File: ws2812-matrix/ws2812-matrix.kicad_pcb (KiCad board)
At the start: 2 copper layers, 80 x 80 mm, 268 parts, among them J1 Conn_01x03, J2 Conn_01x03

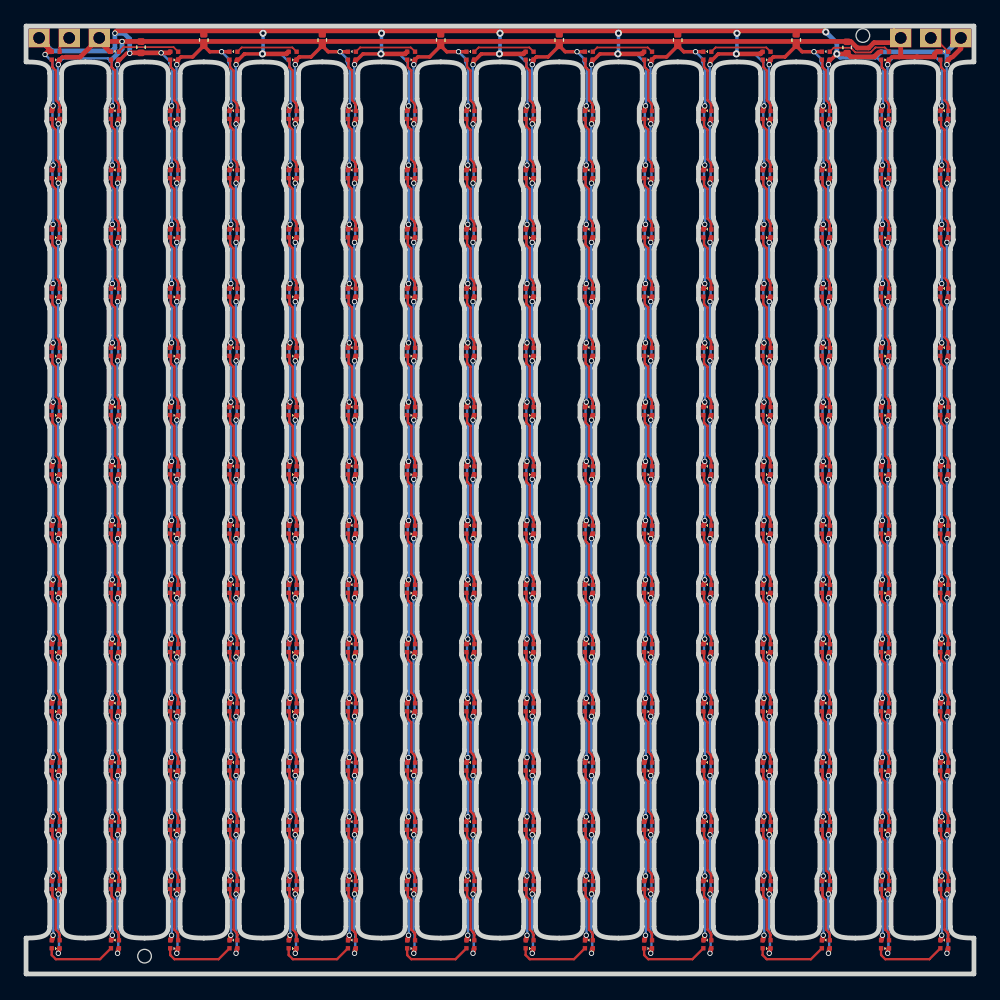
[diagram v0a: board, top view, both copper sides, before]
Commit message: ws2812-matrix: make connectors vertical, increase VCC/GND trace width
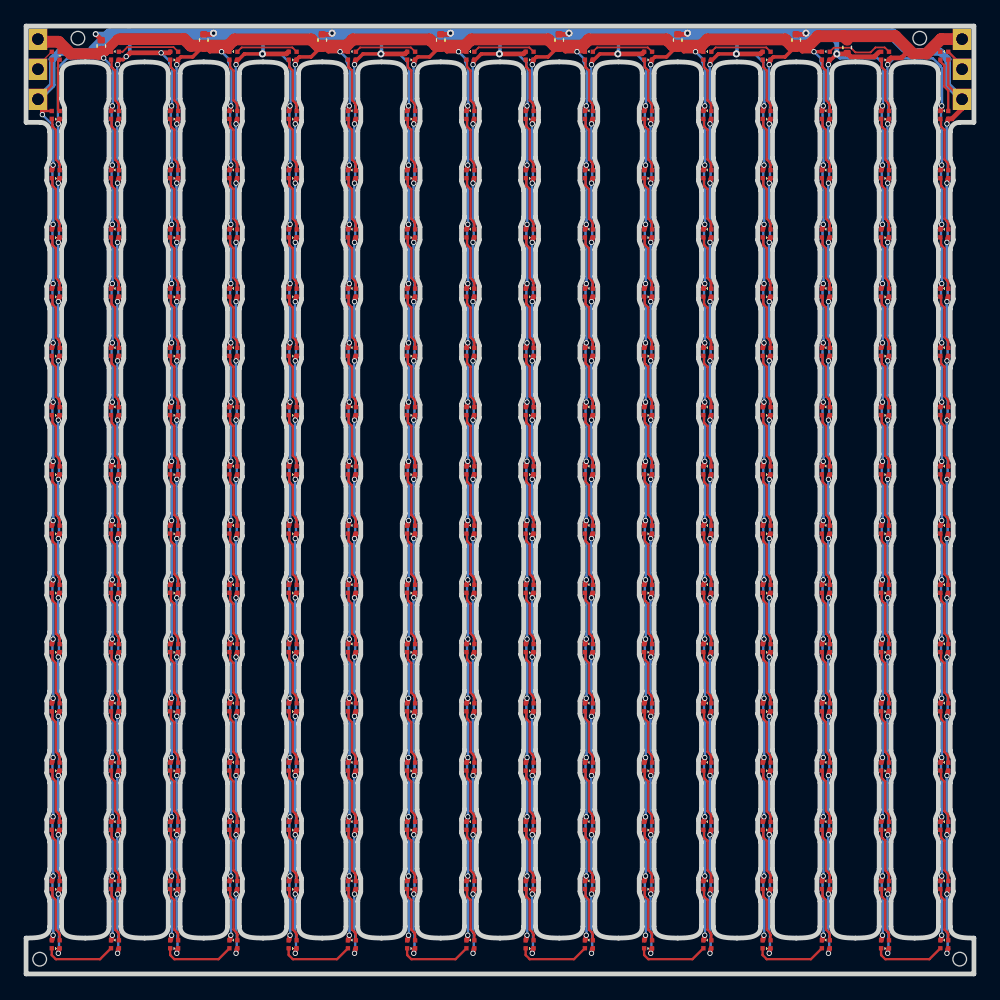
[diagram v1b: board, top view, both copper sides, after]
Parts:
- added REF**: ToolingHole_JLCPCB, Custom:ToolingHole_JLCPCB, F.Cu at (51.9, 48.5)
- added REF**: ToolingHole_JLCPCB, Custom:ToolingHole_JLCPCB, F.Cu at (126.3, 126.2)
- moved REF** 8.85 mm to (48.6, 126.3)
- moved J1 5.18 mm to (48.5, 53.7), turned to 90 degrees
- moved J2 5.18 mm to (126.5, 53.7), turned to 90 degrees
- moved REF** 4.81 mm to (122.9, 48.5)
- moved C1 3.35 mm to (53.9, 49.2), turned to -90 degrees
- turned D1 to -90 degrees
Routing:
- net VCC: track 1351.5 -> 1364.2 mm, vias 264 -> 262
- net GND: track 1336.5 -> 1339.7 mm, vias 255 -> 254
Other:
- outline, holes or cut-outs redrawn

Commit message: ws2812-matrix: switch to SK6805-EC14
This LED is in stock at JLCPCB, unlike the SK6805-EC10.
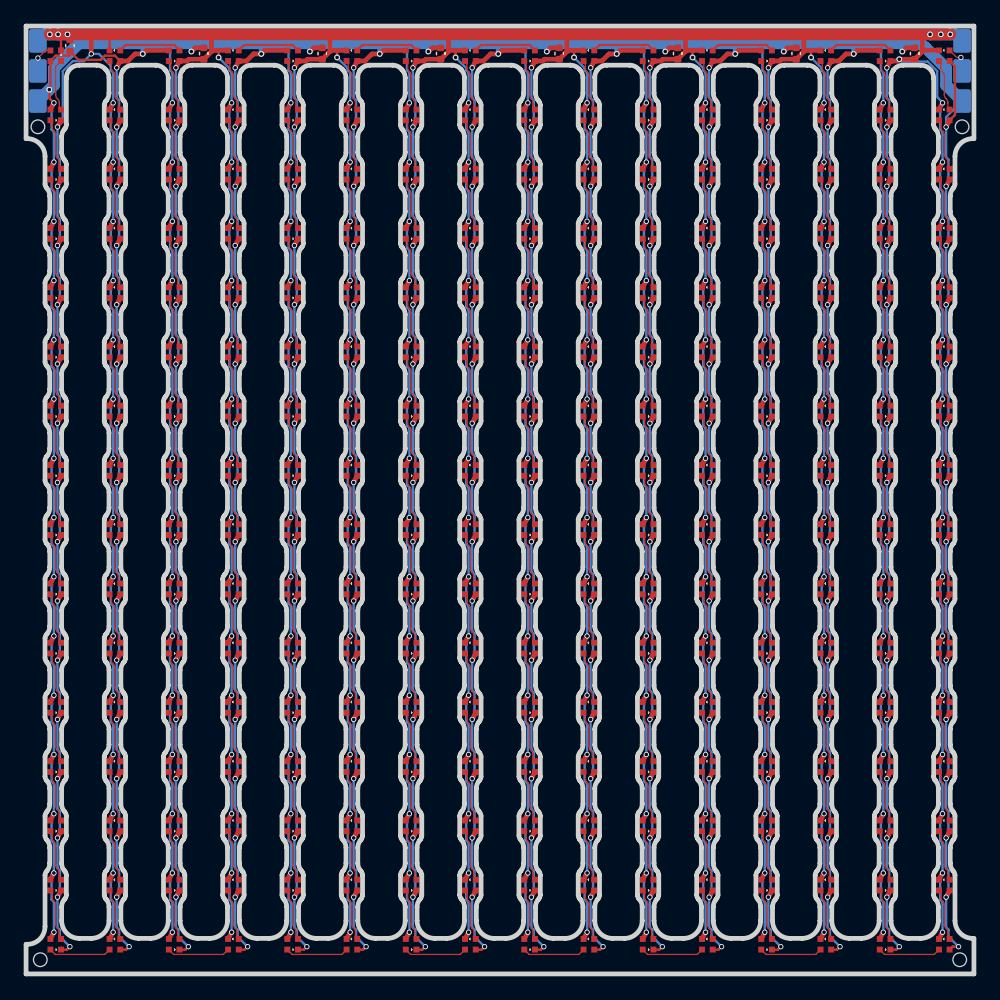
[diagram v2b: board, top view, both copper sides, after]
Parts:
- removed the C8 at (116.8, 49.3)
- added C7: 2.2uF, Capacitor_SMD:C_0402_1005Metric, F.Cu at (112.5, 49.8)
- D1, D10, D100, D101, D102, D103, D104, D105, D106, D107, D108, D109, D11, D110, D111, D112, D113, D114, D115, D116, D117, D118, D119, D12, D120, D121, D122, D123, D124, D125, D126, D127, D128, D129, D13, D130, D131, D132, D133, D134, D135, D136, D137, D138, D139, D14, D140, D141, D142, D143, D144, D145, D146, D147, D148, D149, D15, D150, D151, D152, D153, D154, D155, D156, D157, D158, D159, D16, D160, D161, D162, D163, D164, D165, D166, D167, D168, D169, D17, D170, D171, D172, D173, D174, D175, D176, D177, D178, D179, D18, D180, D181, D182, D183, D184, D185, D186, D187, D188, D189, D19, D190, D191, D192, D193, D194, D195, D196, D197, D198, D199, D2, D20, D200, D201, D202, D203, D204, D205, D206, D207, D208, D209, D21, D210, D211, D212, D213, D214, D215, D216, D217, D218, D219, D22, D220, D221, D222, D223, D224, D225, D226, D227, D228, D229, D23, D230, D231, D232, D233, D234, D235, D236, D237, D238, D239, D24, D240, D241, D242, D243, D244, D245, D246, D247, D248, D249, D25, D250, D251, D252, D253, D254, D255, D256, D26, D27, D28, D29, D3, D30, D31, D32, D33, D34, D35, D36, D37, D38, D39, D4, D40, D41, D42, D43, D44, D45, D46, D47, D48, D49, D5, D50, D51, D52, D53, D54, D55, D56, D57, D58, D59, D6, D60, D61, D62, D63, D64, D65, D66, D67, D68, D69, D7, D70, D71, D72, D73, D74, D75, D76, D77, D78, D79, D8, D80, D81, D82, D83, D84, D85, D86, D87, D88, D89, D9, D90, D91, D92, D93, D94, D95, D96, D97, D98, D99: footprint Custom:SK6805-EC10 -> Custom:SK6805-EC14
- J1, J2: footprint Custom:WS2812-conn -> Custom:WS2812-conn-oneside; moved to B.Cu
- moved C8 10.1 mm to (122.5, 49.8)
- moved REF** 8.29 mm to (126.5, 56.0)
- moved REF** 8.20 mm to (48.5, 56.0)
- moved C1 2.65 mm to (51.2, 49.1), turned to 90 degrees
- moved J1 2.39 mm to (48.5, 51.3)
- moved J2 2.39 mm to (126.5, 51.3)
- moved C2 1.14 mm to (62.5, 49.8)
- moved C3 1.14 mm to (72.5, 49.8)
- moved C4 1.14 mm to (82.5, 49.8)
- moved C5 1.14 mm to (92.5, 49.8)
- moved C6 1.14 mm to (102.5, 49.8)
- moved REF** 0.07 mm to (48.7, 126.3)
- renumbered C7 to C8
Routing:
- net GND: track 1339.7 -> 1370.7 mm, vias 254 -> 261
- net VCC: track 1364.2 -> 1385.0 mm
- net Net-(D241-DIN): track 4.61 -> 2.65 mm
- net Net-(D34-DOUT): track 4.59 -> 2.65 mm
- net Net-(D33-DOUT): track 4.59 -> 2.65 mm
- net Net-(D2-DOUT): track 4.59 -> 2.65 mm
- net Net-(D18-DIN): track 4.59 -> 2.65 mm
- net Net-(D17-DIN): track 4.59 -> 2.65 mm
- net Net-(D226-DOUT): track 4.59 -> 2.65 mm
- net Net-(D209-DIN): track 4.59 -> 2.65 mm
- net Net-(D177-DIN): track 4.59 -> 2.65 mm
- net Net-(D161-DOUT): track 4.59 -> 2.65 mm
- net Net-(D145-DIN): track 4.59 -> 2.65 mm
- net Net-(D130-DOUT): track 4.59 -> 2.65 mm
- net Net-(D98-DOUT): track 4.59 -> 2.65 mm
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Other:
- outline, holes or cut-outs redrawn
- board text added: "aykevl.nl - 16x16 LED matrix SK6805-EC14 v0.1"
- board text removed: "aykevl.nl - 16x16 LED matrix SK6805-EC10 v0.1"
